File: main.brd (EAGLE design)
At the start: 160 x 100 mm, 0 parts

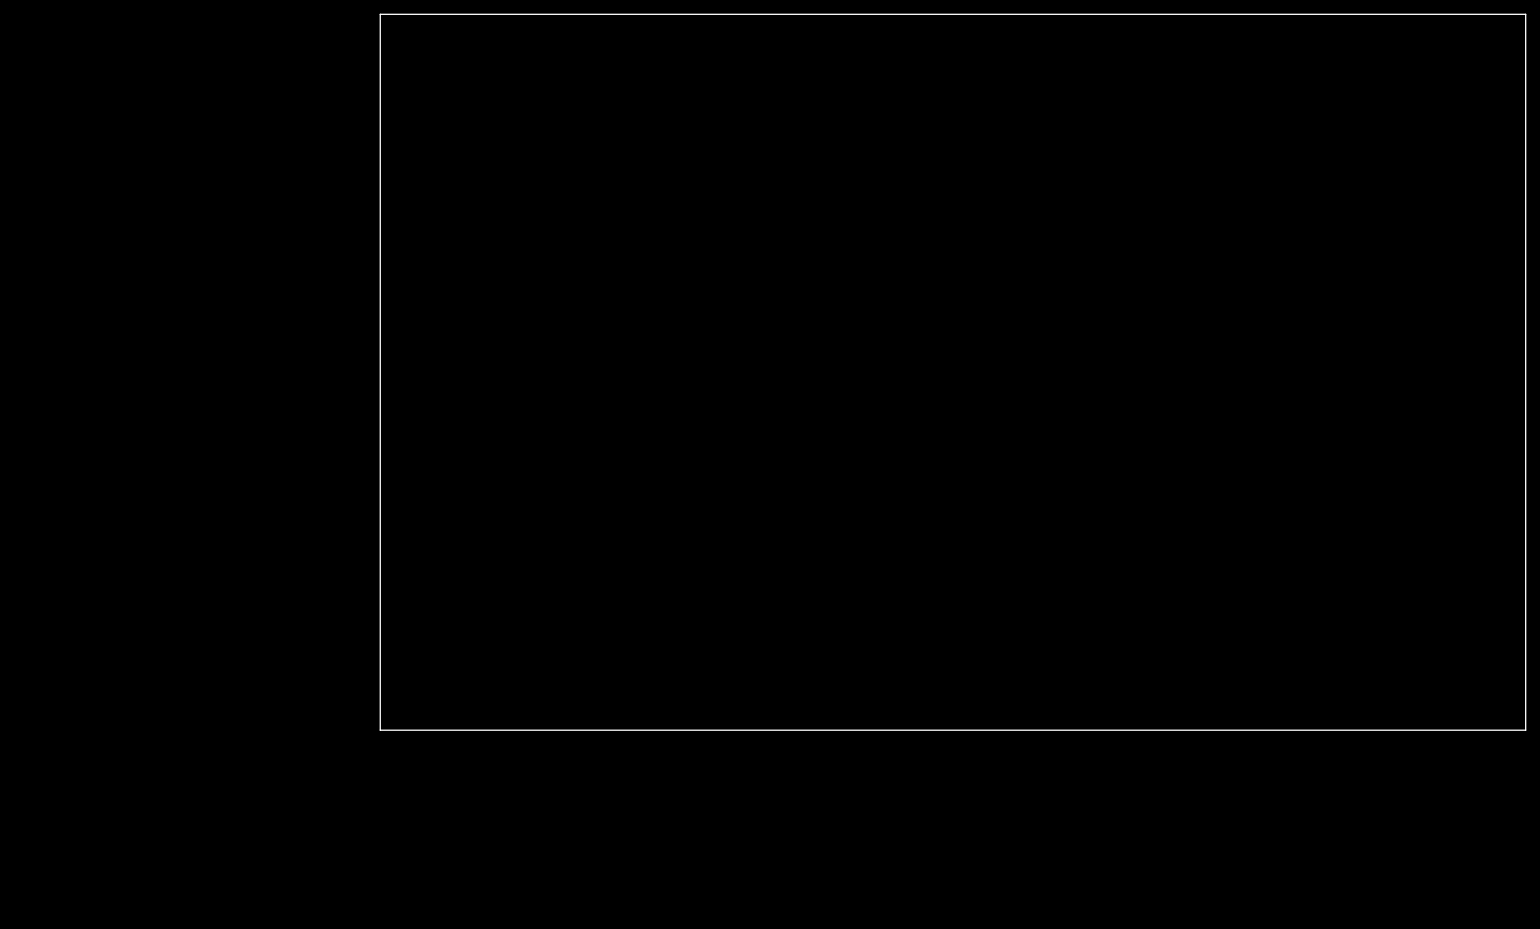
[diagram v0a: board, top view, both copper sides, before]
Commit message: Outline, mounting holes and groundplanes
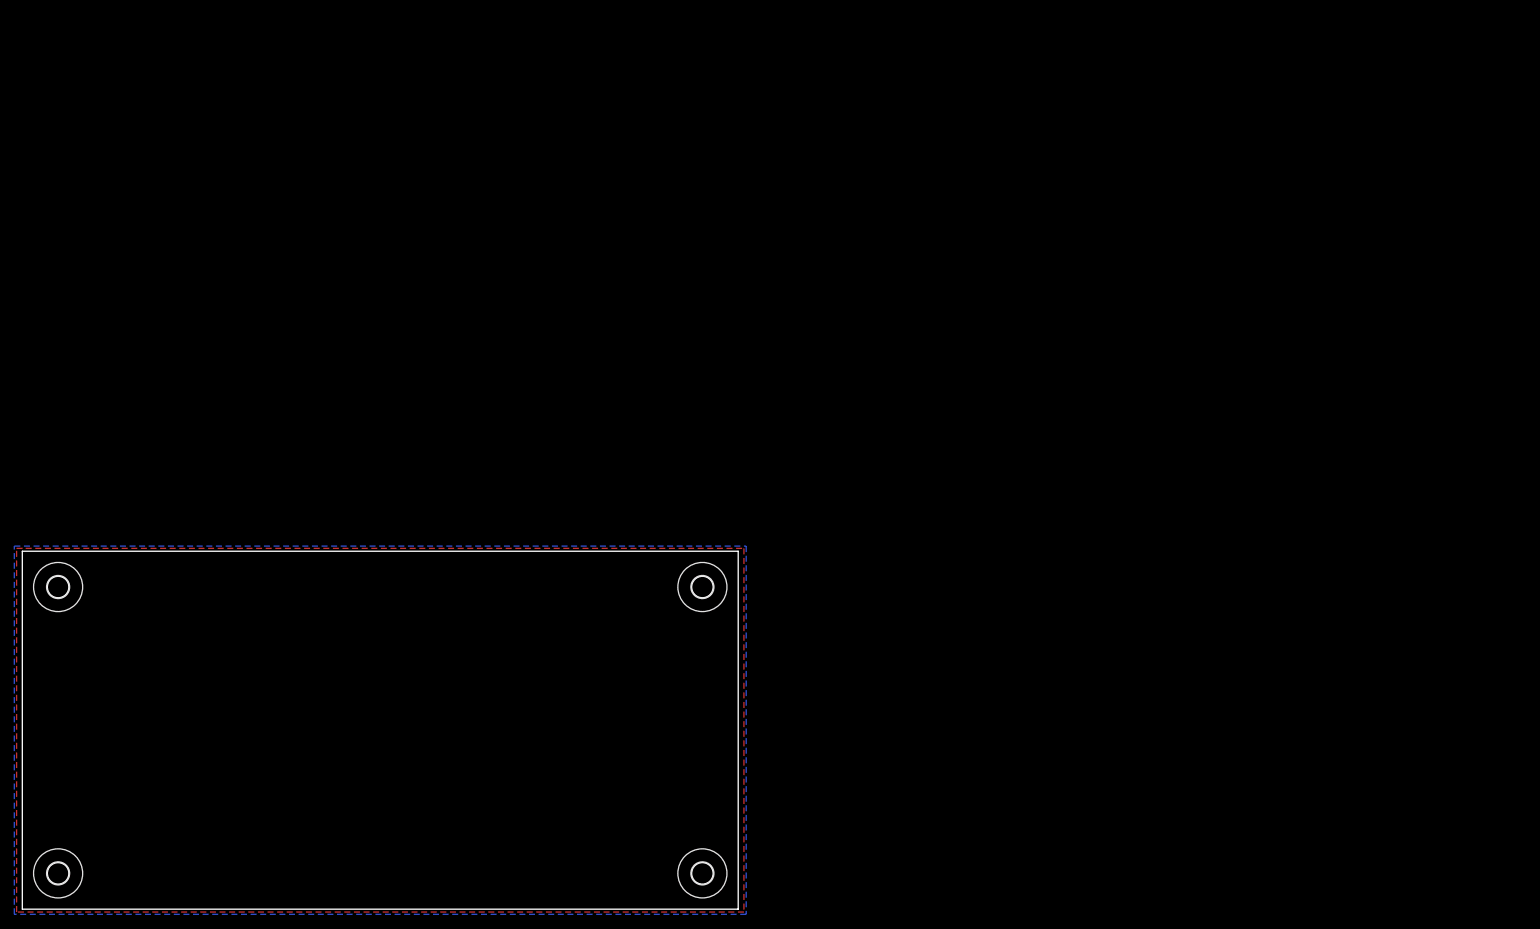
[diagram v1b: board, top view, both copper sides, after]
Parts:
- added H1, H2, H3, H4: MOUNT-HOLE3.0, holes:3,0
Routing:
- added copper zone on layer 1, net GND
- added copper zone on layer 16, net GND
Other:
- board size 160 x 100 mm -> 100 x 50 mm
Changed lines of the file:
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@@
 <setting verticaltext="up"/>
 </settings>
-<grid distance="50" unitdist="mil" unit="mil" style="lines" multiple="1" display="no" altdistance="5" altunitdist="mil" altunit="mil"/>
+<grid distance="12.5" unitdist="mil" unit="mil" style="lines" multiple="1" display="no" altdistance="5" altunitdist="mil" altunit="mil"/>
 <layers>
 <layer number="1" name="Top" color="4" fill="1" visible="yes" active="yes"/>
@@
 <board>
 <plain>
-<wire x1="0" y1="0" x2="160" y2="0" width="0" layer="20"/>
-<wire x1="160" y1="0" x2="160" y2="100" width="0" layer="20"/>
-<wire x1="160" y1="100" x2="0" y2="100" width="0" layer="20"/>
-<wire x1="0" y1="100" x2="0" y2="0" width="0" layer="20"/>
+<wire x1="-50" y1="-25" x2="50" y2="-25" width="0" layer="20"/>
+<wire x1="50" y1="-25" x2="50" y2="25" width="0" layer="20"/>
+<wire x1="50" y1="25" x2="-50" y2="25" width="0" layer="20"/>
+<wire x1="-50" y1="25" x2="-50" y2="-25" width="0" layer="20"/>
 </plain>
 <attributes>
@@
 </autorouter>
 <elements>
+<element name="H1" library="holes" library_urn="urn:adsk.eagle:library:237" package="3,0" package3d_urn="urn:adsk.eagle:package:14277/1" value="MOUNT-HOLE3.0" x="-45" y="20" locked="yes" smashed="yes"/>
+<element name="H2" library="holes" library_urn="urn:adsk.eagle:library:237" package="3,0" package3d_urn="urn:adsk.eagle:package:14277/1" value="MOUNT-HOLE3.0" x="-45" y="-20" locked="yes" smashed="yes"/>
+<element name="H3" library="holes" library_urn="urn:adsk.eagle:library:237" package="3,0" package3d_urn="urn:adsk.eagle:package:14277/1" value="MOUNT-HOLE3.0" x="45" y="-20" locked="yes" smashed="yes"/>
+<element name="H4" library="holes" library_urn="urn:adsk.eagle:library:237" package="3,0" package3d_urn="urn:adsk.eagle:package:14277/1" value="MOUNT-HOLE3.0" x="45" y="20" locked="yes" smashed="yes"/>
 </elements>
 <signals>
+<signal name="GND">
+<polygon width="0.1524" layer="1">
+<vertex x="-49.53" y="25.4"/>
+<vertex x="50.8" y="25.4"/>
+<vertex x="50.8" y="-25.4"/>
+<vertex x="-50.8" y="-25.4"/>
+<vertex x="-50.8" y="25.4"/>
+</polygon>
+<polygon width="0.1524" layer="16">
+<vertex x="-51.1175" y="25.7175"/>
+<vertex x="51.1175" y="25.7175"/>
+<vertex x="51.1175" y="-25.7175"/>
+<vertex x="-51.1175" y="-25.7175"/>
+</polygon>
+</signal>
 </signals>
 <mfgpreviewcolors>
@@
 </board>
 </drawing>
+<compatibility>
+<note version="8.2" severity="warning">
+Since Version 8.2, EAGLE supports online libraries. The ids
+of those online libraries will not be understood (or retained)
+with this version.
+</note>
+<note version="8.3" severity="warning">
+Since Version 8.3, EAGLE supports URNs for individual library
+assets (packages, symbols, and devices). The URNs of those assets
+will not be understood (or retained) with this version.
+</note>
+<note version="8.3" severity="warning">
+Since Version 8.3, EAGLE supports the association of 3D packages
+with devices in libraries, schematics, and board files. Those 3D
+packages will not be understood (or retained) with this version.
+</note>
+</compatibility>
 </eagle>

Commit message: Added initial components
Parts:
- added C1: 100n, resistor:C0805
- added C12, C2, C3, C4, C56, C62: 100nF, resistor:C0805
- added C5, C58, C61: 1uF_X5R, resistor:C0805
- added C57: 10nF X7R, resistor:C0805
- added C59, C60: 10uF, resistor:SMC_C
- added D1: BAT54S, diode:SOT23
- added D14: BAT60JFILM, diode:SOD323-W
- added IC17: LD398533RM, st-microelectronics:SOT23-5L
- added IC18: LD1117S50TR, v-reg:SOT223
- added J1: DCJ0202, con-jack:DCJ0202
- added LED1, LED14: ROOD, led:CHIP-LED0805
- added R1: 10K, resistor:R0805
- added R2, R39, R6, R7, R8: 1K, resistor:R0805
- added R3, R4, R5: 4K7, resistor:R0805
- added S1: (no value), switch-omron:B3F-10XX
- added U1: TMP275AIDR, TMP275AIDR:SOIC127P600X175-8N
- added U4: ESP-WROOM-32, esp32:ESP-WROOM-32
- added X1: 1751251, con-phoenix-350:1751251
- added X2: 87438-02, con-molex:87438-02
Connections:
- new net +12V: C59.+, IC18.3, J1.1, X2.2
- new net +3V3: C12.1, C4.1, C5.1, C61.1, C62.1, D1.2, IC17.5, R1.2, R3.2, R4.2, R5.2, R7.2, R8.2, U1.8, U4.2
- new net +5V: C60.+, D14.A, IC18.4, R39.2
- new net BTN: C2.1, R8.1, S1.2
- new net GND: C1.2, C12.2, C2.2, C3.2, C4.2, C5.2, C56.2, C57.2, C58.2, C59.-, C60.-, C61.2, C62.2, D1.1, IC17.2, IC18.1, J1.3, LED1.C, LED14.C, S1.3, U1.4, U1.5, U1.6, U1.7, U4.1, U4.15, U4.38, X2.1
- new net I2C_SCL: R3.1, U1.2
- new net I2C_SDA: R4.1, U1.1
- new net LED: R6.2
- new net N$1: C1.1, D1.3, R1.1, R2.2
- new net N$102: C57.1, IC17.4
- new net N$113: C56.1, C58.1, D14.C, IC17.1, IC17.3
- new net N$2: R2.1
- new net N$5: LED1.A, R6.1
- new net N$6: C3.1, R7.1, U4.3
- new net N$99: LED14.A, R39.1
- new net RDX0: U4.34
- new net TEMP_ALERT: R5.1, U1.3
- new net TXD0: U4.35
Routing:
- net N$113: track 0.00 -> 8.37 mm
- net +3V3: track 0.00 -> 4.53 mm

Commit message: Update :)
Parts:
- added C10, C7, C9: 100n, resistor:C0805
- added C6, C8: 10nF X7R, resistor:C0805
- added D2: BAT54S, diode:SOT23
- added D3: BAT60JFILM, diode:SOD323-W
- added IC1, IC2: PM8834-SO08N, PM8834:SO08N
- added JP1: (no value), pinhead:1X06
- added Q1, Q2, Q3, Q4: IRF3205SPBF, IRF3205SPBF:TRANS_IRF3205SPBF
- added R10: 1K, resistor:R0805
- added R11, R12, R13, R14, R9: 10K, resistor:R0805
- added X3: 1751251, con-phoenix-350:1751251
- added X4: 1751277, con-phoenix-350:1751277
- moved C12 72.9 mm to (-21.6, 44.5)
- moved R3 72.9 mm to (-17.8, 38.4)
- moved R4 72.9 mm to (-20.0, 38.4)
- moved R5 72.9 mm to (-15.6, 38.4)
- moved U1 72.9 mm to (-17.8, 44.5)
- moved X2 71.7 mm to (-27.9, -50.8), turned to 90 degrees
- moved C57 70.0 mm to (-69.5, -48.3), turned to 180 degrees
- moved D14 69.1 mm to (-60.3, -50.5), turned to 0 degrees
- moved C56 67.2 mm to (-66.7, -51.4), turned to 270 degrees
- moved C58 67.2 mm to (-64.1, -51.4), turned to 270 degrees
- moved C61 67.2 mm to (-72.4, -51.4)
- moved C62 67.2 mm to (-74.6, -51.4)
- moved IC17 67.2 mm to (-69.5, -51.4)
- moved J1 63.4 mm to (-35.6, -44.5), turned to 0 degrees
- moved R39 52.8 mm to (-60.3, -52.7), turned to 0 degrees
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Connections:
- net N$1 renamed INP2
- new net CTS: JP1.6
- new net INP1: C10.1, D2.3, R10.2, R9.1
- new net N$1: R11.2
- new net N$10: IC1.1, IC2.1, R11.1, R13.1
- new net N$12: IC1.7, Q2.1
- new net N$13: IC1.5, Q1.1
- new net N$14: Q2.2, X4.3
- new net N$15: IC2.7, Q4.1
- new net N$16: IC2.5, Q3.1
- new net N$17: Q3.2, X4.4
- new net N$18: Q4.2, X4.5
- new net N$19: R12.2
- new net N$20: R10.1, X3.2
- new net N$22: X3.1
- new net N$23: R14.2
- new net N$24: R13.2
- new net N$4: X1.1
- new net N$7: Q1.2, X4.2
- new net N$9: IC1.4, IC2.4
- new net PWM1: IC1.2
- new net PWM2: IC1.8, R12.1
- new net PWM3: IC2.2
- new net PWM4: IC2.8, R14.1
- new net RTS: JP1.5
- new net UART_5V: D3.A, JP1.1
- net +12V: now also C6.1, C7.1, C8.1, C9.1, IC1.6, IC2.6, X4.1
- net +3V3: now also D2.2, R9.2
- net GND: now also C10.2, C6.2, C7.2, C8.2, C9.2, D2.1, IC1.3, IC2.3, JP1.2, Q1.3, Q2.3, Q3.3, Q4.3, X1.3, X3.3
- net N$113: now also D3.C
- net N$2: now also X1.2
- net RDX0: now also JP1.4
- net TXD0: now also JP1.3
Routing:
- net N$7: track 0.00 -> 21.6 mm
- net N$18: track 0.00 -> 18.8 mm
- net +3V3: track 4.53 -> 23.1 mm, vias 0 -> 2
- net N$14: track 0.00 -> 13.2 mm
- net N$17: track 0.00 -> 11.1 mm
- net INP1: track 0.00 -> 8.11 mm
- net N$20: track 0.00 -> 6.29 mm
- net N$2: track 0.00 -> 6.29 mm
- net INP2: track 0.00 -> 5.84 mm
- net +5V: track 0.00 -> 5.67 mm
- net +12V: track 0.00 -> 5.59 mm
- net N$102: track 0.00 -> 2.03 mm
- added copper zone on layer 1, net +12V

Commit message: layouting
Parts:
- removed X2: 87438-02, con-molex:87438-02
- added D4: TSOP57238TT1, SparkFun-Sensors:TSOP572
- added R15, R16: 1K, resistor:R0805
- added U2: SI7021, SparkFun-Sensors:DFN-6-3X3-SI7021
- moved LED14 70.2 mm to (-0.95, -17.1), turned to 0 degrees
- moved C6 67.2 mm to (16.8, -8.26)
- moved C7 67.2 mm to (16.8, -6.03)
- moved C8 67.2 mm to (16.8, 4.76)
- moved C9 67.2 mm to (16.8, 2.54)
- moved IC1 67.2 mm to (16.8, -1.59)
- moved IC2 67.2 mm to (16.8, 8.89)
- moved R11 67.2 mm to (10.8, 10.8)
- moved R12 67.2 mm to (10.5, 2.54)
- moved R13 67.2 mm to (10.5, 0.32)
- moved R14 67.2 mm to (10.8, 13.0)
- moved R39 67.2 mm to (-0.95, -21.3), turned to 270 degrees
- moved C60 65.3 mm to (4.76, -21.9), turned to 0 degrees
- moved IC18 63.3 mm to (4.76, -16.5), turned to 90 degrees
- moved C58 62.9 mm to (-8.89, -21.3)
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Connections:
- removed net PWM4: IC2.8, R14.1
- new net PWM0: IC1.2, U4.30
- new net VDD: U2.VDD
- net +12V: no longer X2.2
- net GND: now also R15.1, R16.1, U2.GND; no longer X2.1
- net N$2: now also R15.2
- net N$20: now also R16.2
- net PWM1: now also IC1.8, R12.1, U4.31; no longer IC1.2
- net PWM2: now also IC2.2, U4.36; no longer IC1.8, R12.1
- net PWM3: now also IC2.8, R14.1, U4.37; no longer IC2.2
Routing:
- net +12V: track 5.59 -> 71.6 mm
- net N$13: track 0.00 -> 14.2 mm
- net N$15: track 0.00 -> 13.9 mm
- net PWM1: track 0.00 -> 9.75 mm, vias 0 -> 2
- net PWM3: track 0.00 -> 9.44 mm, vias 0 -> 2
- net +3V3: track 23.1 -> 31.5 mm
- net N$12: track 0.00 -> 6.28 mm
- net N$16: track 0.00 -> 4.96 mm
- net N$10: track 0.00 -> 4.68 mm
- net TEMP_ALERT: track 0.00 -> 3.01 mm
- net I2C_SDA: track 0.00 -> 3.01 mm
- net I2C_SCL: track 0.00 -> 2.62 mm
- net INP2: track 5.84 -> 8.42 mm
- net N$2: track 6.29 -> 8.72 mm
- net N$99: track 0.00 -> 2.13 mm
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- removed copper zone on layer 1, net +12V

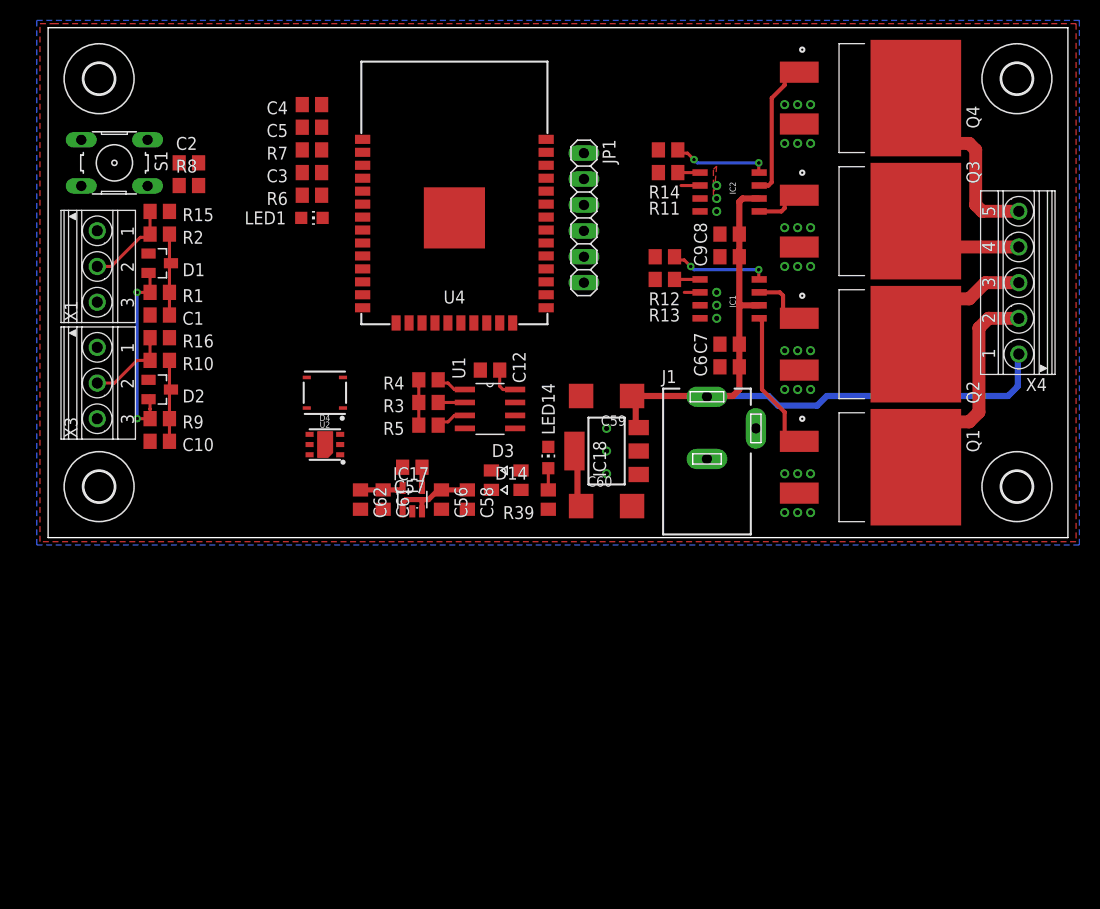
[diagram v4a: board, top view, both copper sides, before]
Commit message: added level shifters
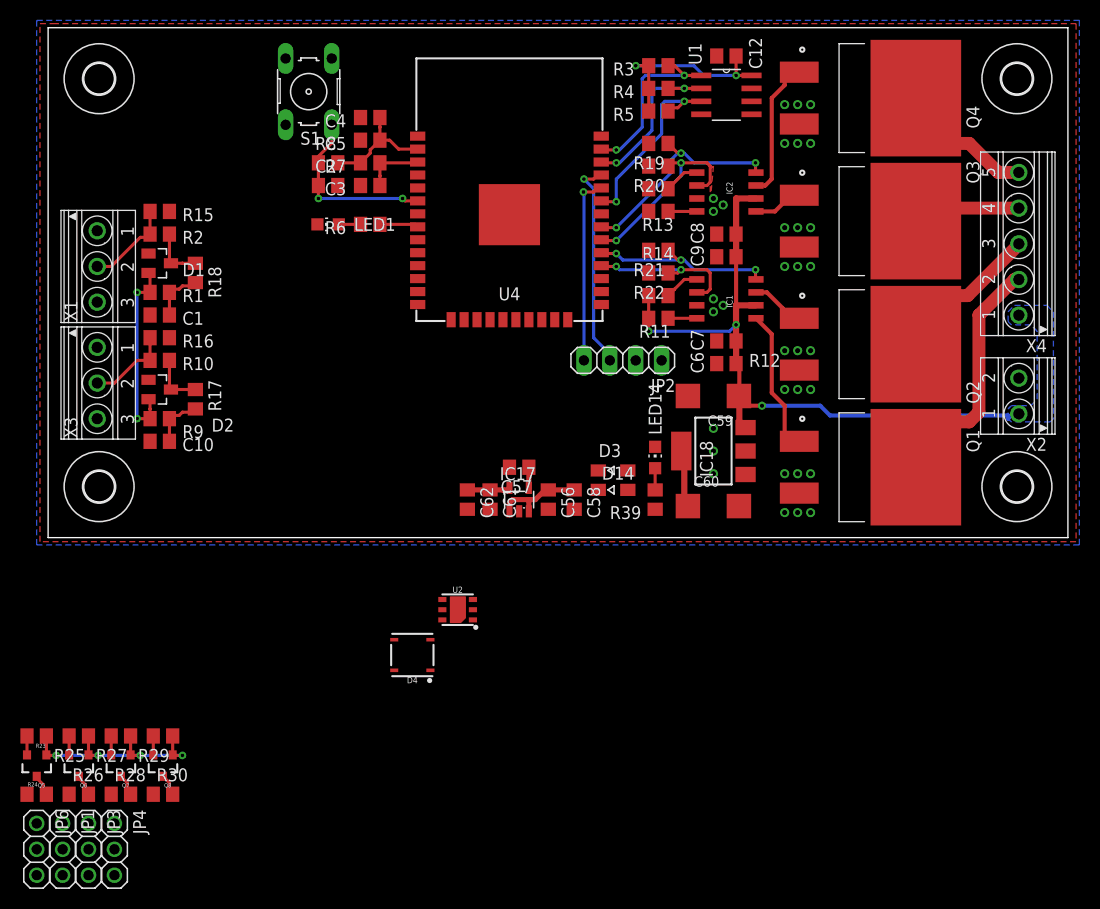
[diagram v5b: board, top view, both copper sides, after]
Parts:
- removed J1: DCJ0202, con-jack:DCJ0202
- added JP2: (no value), pinhead:1X04
- added JP3, JP4, JP6: (no value), adafruit:1X03
- added Q5, Q6, Q7, Q8: BSS138, SparkFun:SOT23-3
- added R17, R18: 1K, resistor:R0805
- added R19, R20, R21, R22, R23, R24, R25, R26, R27, R28, R29, R30: 10K, resistor:R0805
- added X2: 1751248, con-phoenix-350:1751248
- JP1: device pinhead:1X06 -> adafruit:1X03
- R10, R2: value 1K -> 10R
- R15, R16: value 1K -> X
- moved JP1 80.3 mm to (-48.6, -55.6)
- moved R3 40.0 mm to (9.84, 21.3)
- moved C12 38.5 mm to (16.5, 22.2)
- moved U1 38.5 mm to (16.5, 18.4)
- moved R5 38.2 mm to (9.84, 16.8)
- moved R4 36.4 mm to (9.84, 19.1)
- moved D4 27.1 mm to (-14.3, -36.5)
- moved U2 20.8 mm to (-9.84, -32.1)
- moved S1 20.3 mm to (-24.4, 18.7), turned to 270 degrees
- moved C2 13.8 mm to (-22.5, 9.53)
- moved R8 13.8 mm to (-22.5, 11.7)
- moved R11 12.1 mm to (9.84, -1.27)
- moved C58 10.5 mm to (1.59, -21.3)
- moved LED14 10.5 mm to (9.53, -17.1)
- moved R39 10.5 mm to (9.53, -21.3)
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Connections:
- removed net CTS: JP1.6
- removed net N$1: R11.2
- removed net N$19: R12.2
- removed net N$23: R14.2
- removed net N$24: R13.2
- removed net RTS: JP1.5
- new net HV: JP1.1, JP3.1, JP4.1, JP6.1, R24.1, R26.1, R28.1, R30.1
- new net HV1: JP6.2, Q5.3, R24.2
- new net HV2: JP1.2, Q6.3, R26.2
- new net HV3: JP3.2, Q7.3, R28.2
- new net HV4: JP4.2, Q8.3, R30.2
- new net LV0: Q5.2, R23.2
- new net LV1: Q6.2, R25.2
- new net LV2: Q7.2, R27.2
- new net LV3: Q8.2, R29.2
- new net N$2001: IC2.4, R14.1
- new net N$2OO: IC2.1, R13.1
- new net N$3: D2.3, R10.2, R17.1
- new net N$8: D1.3, R18.1, R2.2
- net +12V: now also R11.2, R12.2, X2.1; no longer J1.1
- net +3V3: now also Q5.1, Q6.1, Q7.1, Q8.1, R23.1, R25.1, R27.1, R29.1
- net BTN: now also U4.6
- net GND: now also JP1.3, JP2.2, JP3.3, JP4.3, JP6.3, R13.2, R14.2, R19.2, R20.2, R21.2, R22.2, X2.2; no longer J1.3, JP1.2
- net I2C_SCL: now also R4.1, U4.36; no longer R3.1
- net I2C_SDA: now also R3.1, U4.37; no longer R4.1
- net INP1: now also R17.2, U4.10; no longer D2.3, R10.2
- net INP2: now also R18.2, U4.9; no longer D1.3, R2.2
- net LED: now also U4.8
- net N$10: no longer IC2.1, R13.1
- net N$9: now also R12.1; no longer IC2.4
- net PWM0: now also R22.1, U4.28; no longer U4.30
- net PWM1: now also R21.1, U4.29; no longer R12.1, U4.31
- net PWM2: now also R20.1, U4.30; no longer U4.36
- net PWM3: now also R19.1, U4.31; no longer R14.1, U4.37
- net RDX0: now also JP2.4; no longer JP1.4
- net TEMP_ALERT: now also U4.33
- net TXD0: now also JP2.3; no longer JP1.3
- net UART_5V: now also JP2.1; no longer JP1.1
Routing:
- net +3V3: track 31.5 -> 78.5 mm, vias 2 -> 8
- net TXD0: track 0.00 -> 20.7 mm, vias 0 -> 1
- net RDX0: track 0.00 -> 18.5 mm, vias 0 -> 1
- net BTN: track 0.00 -> 17.6 mm, vias 0 -> 2
- net PWM2: track 1.86 -> 19.2 mm, vias 0 -> 2
- net TEMP_ALERT: track 3.01 -> 18.9 mm, vias 0 -> 2
- net I2C_SDA: track 3.01 -> 17.6 mm, vias 0 -> 2
- net I2C_SCL: track 2.62 -> 16.6 mm, vias 0 -> 2
- net PWM0: track 1.54 -> 15.4 mm, vias 0 -> 2
- net PWM3: track 9.44 -> 22.0 mm, vias 2 -> 3
- net PWM1: track 9.75 -> 18.5 mm, vias 2 -> 3
- net N$6: track 0.00 -> 5.96 mm
- net N$3: track 0.00 -> 5.61 mm
- net N$8: track 0.00 -> 5.52 mm
- net N$18: track 18.8 -> 14.1 mm
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- added copper zone on layer 16, net +12V
